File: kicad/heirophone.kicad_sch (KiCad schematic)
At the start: 127 parts, among them J1 AudioJack2_SwitchT, J10 Conn_01x02, J11 Conn_01x02, J12 Conn_01x02, J2 AudioJack2_SwitchT, J4 AudioJack2_SwitchT, J5 AudioJack2_SwitchT, J6 AudioJack2_SwitchT, J7 AudioJack2_SwitchT, J9 Conn_01x02, Q1 2N3904, Q2 2N3906, Q3 2N3906, SW2 SW_SPDT, SW3 SW_SPDT, U10 TL072, U11 TL072, U12 TL072, U13 TL072, U2 LM13700, U3 LM13700, U4 TL072, U5 TL072, U6 LM386, U7 NE5534, U8 TL072

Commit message: Updating kicad project with new name
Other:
- title: Steel Plate Feedback -> Heirophone

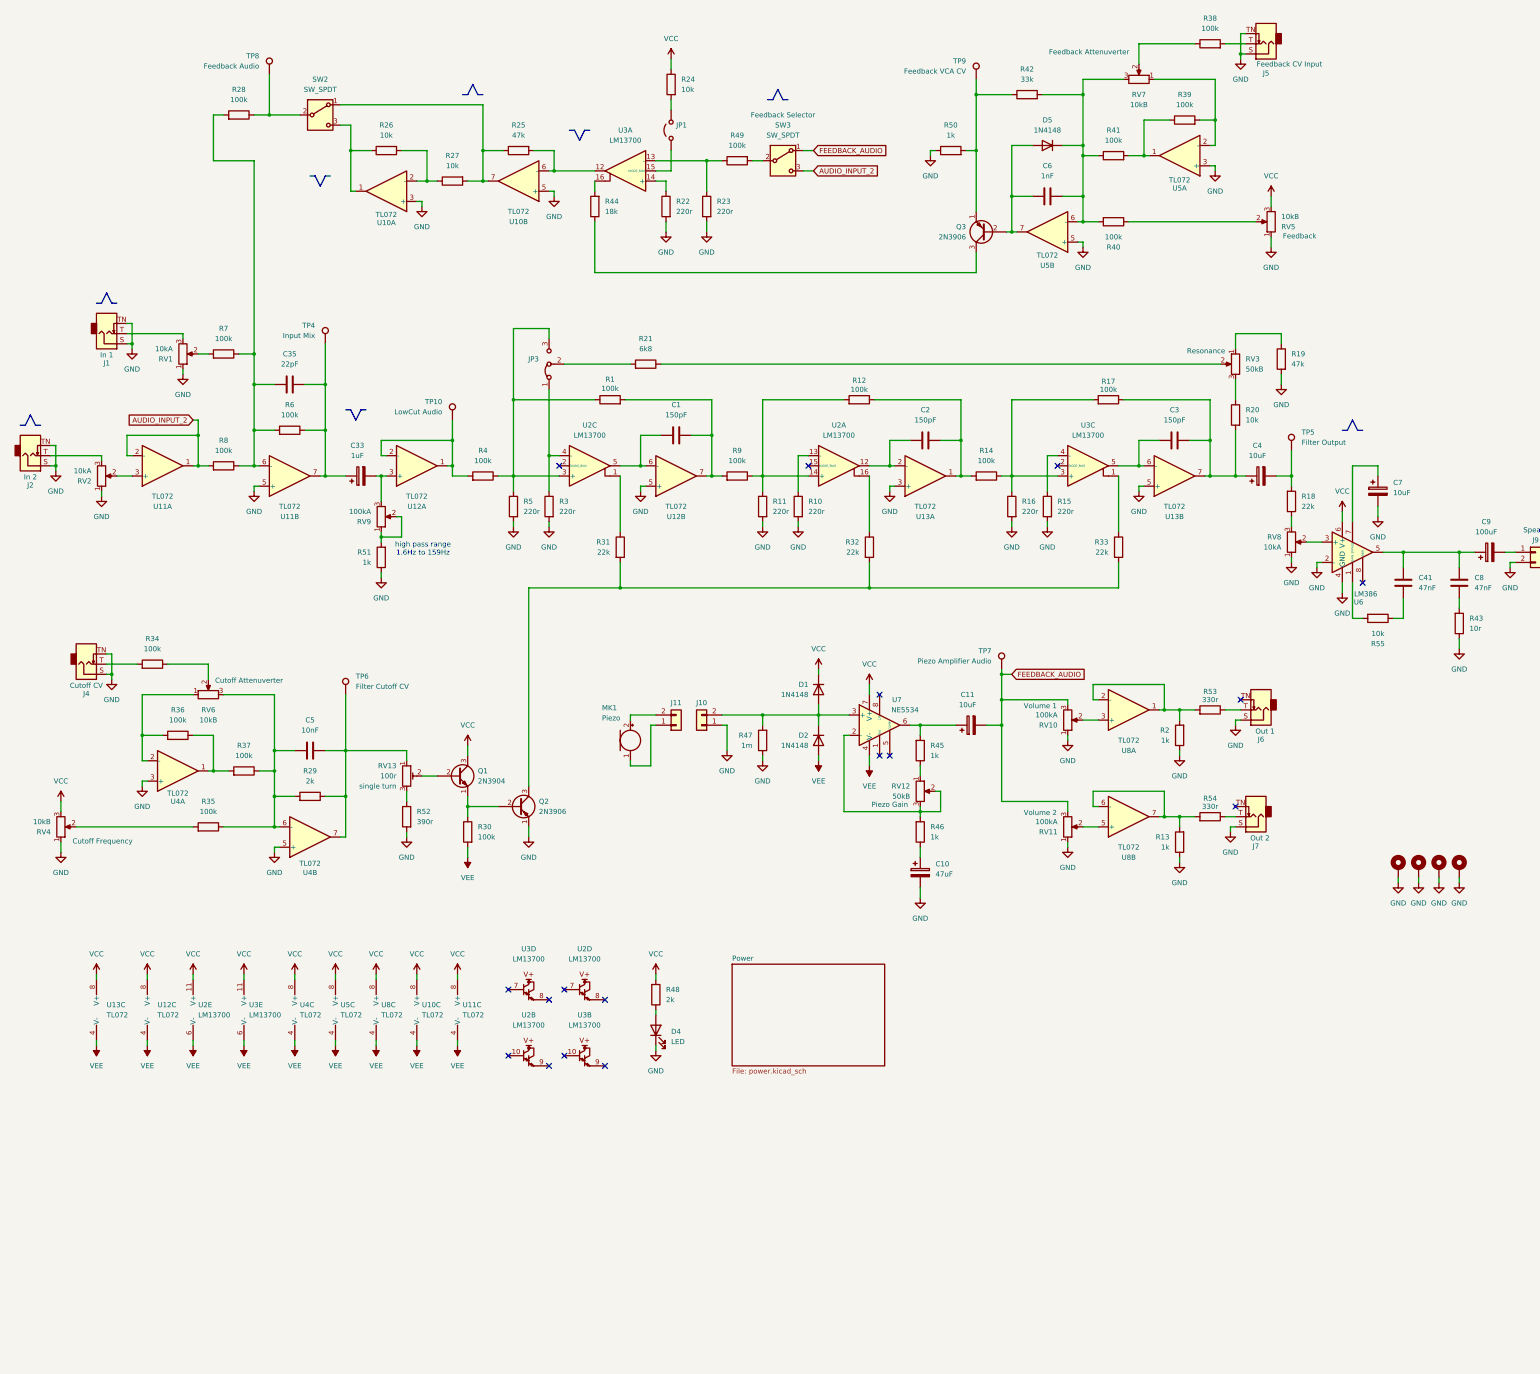
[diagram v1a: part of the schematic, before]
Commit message: Redesign feedback VCA to be a multiplier
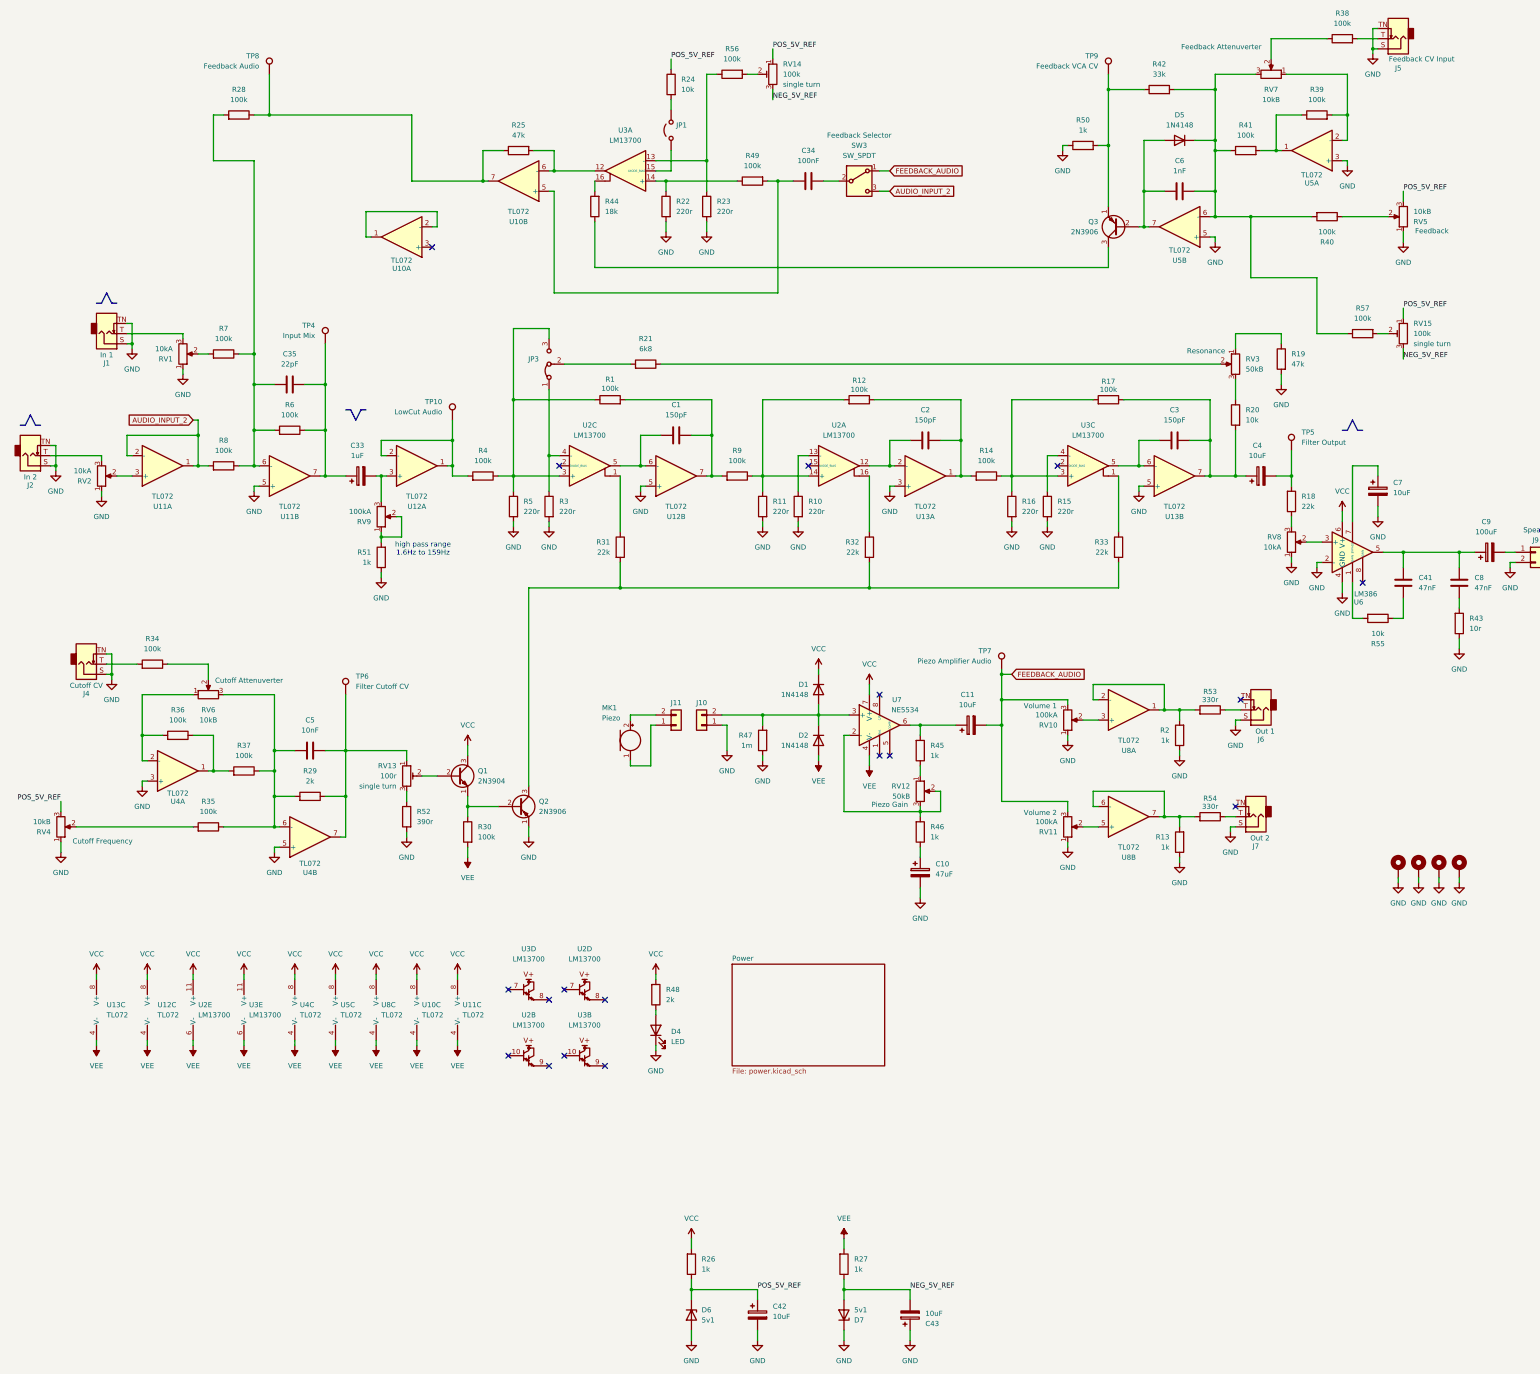
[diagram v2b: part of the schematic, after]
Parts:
- removed SW2: SW_SPDT, Rumblesan_Standard_Parts:Toggle_Switch_100SP-M2, symbol Switch:SW_SPDT
- added C34: 100nF, Rumblesan_Standard_Parts:C_Rect_L7.0mm_W2.5mm_P5.00mm, symbol Rumblesan_Standard_Parts:C
- added C42, C43: 10uF, Rumblesan_Standard_Parts:CP_Radial_D5.0mm_P2.00mm, symbol Rumblesan_Standard_Parts:C_Polarized
- added D6, D7: 5v1, Diode_THT:D_DO-41_SOD81_P10.16mm_Horizontal, symbol Device:D_Zener
- added R56, R57: 100k, Rumblesan_Standard_Parts:R_Axial_DIN0207_L6.3mm_D2.5mm_P10.16mm_Horizontal, symbol Rumblesan_Standard_Parts:R
- added RV14, RV15: 100k, Rumblesan_Potentiometer_THT:Potentiometer_THT_Bourns_3306P_Vertical, symbol Rumblesan_Standard_Parts:R_Potentiometer_Trim
- R26, R27: value 10k -> 1k
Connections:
- net GND: now also C42.2, C43.1, D6.2 (A), D7.1 (K); no longer U10.3 (+), U10.5 (+)
- net VCC: now also R26.1; no longer R24.2, RV4.3, RV5.3
- net VEE: now also R27.1
- net at C6.1, D5.1 (K), R40.1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: now also R57.2
- net at R28.2, TP8.1: now also R25.2, U10.7
- net at U10.1: now also U10.2 (-); no longer R26.2
- net at R22.2, U3.14 (+): now also R49.2
- net at R23.2, U3.13 (-): now also R56.2; no longer R49.2
- net at R49.1: now also U10.5 (+), C34.1; no longer SW3.2 (B)
- new net: R57.1, RV15.2
- new net: C34.2, SW3.2 (B)
- new net: R56.1, RV14.2
- new net NEG_5V_REF: C43.2, D7.2 (A), R27.2, RV14.3, RV15.3
- new net POS_5V_REF: C42.1, D6.1 (K), R24.2, R26.2, RV14.1, RV15.1, RV4.3, RV5.3
- no-connect marks 17 -> 18
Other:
- moved on the sheet: C6, D5, J5, Q3, R38, R39, R40, R41, R42, R49, R50, RV5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
